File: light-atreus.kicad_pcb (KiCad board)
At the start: 2 copper layers, 40.1 x 44.5 mm, 10 parts, among them J1 USB_B, J11 USB_B, J2 CONN_01X02, J3 CONN_01X02, J4 CONN_01X02, J5 CONN_01X02, J6 CONN_01X02, J7 CONN_01X02, J8 CONN_01X02, J9 CONN_01X02

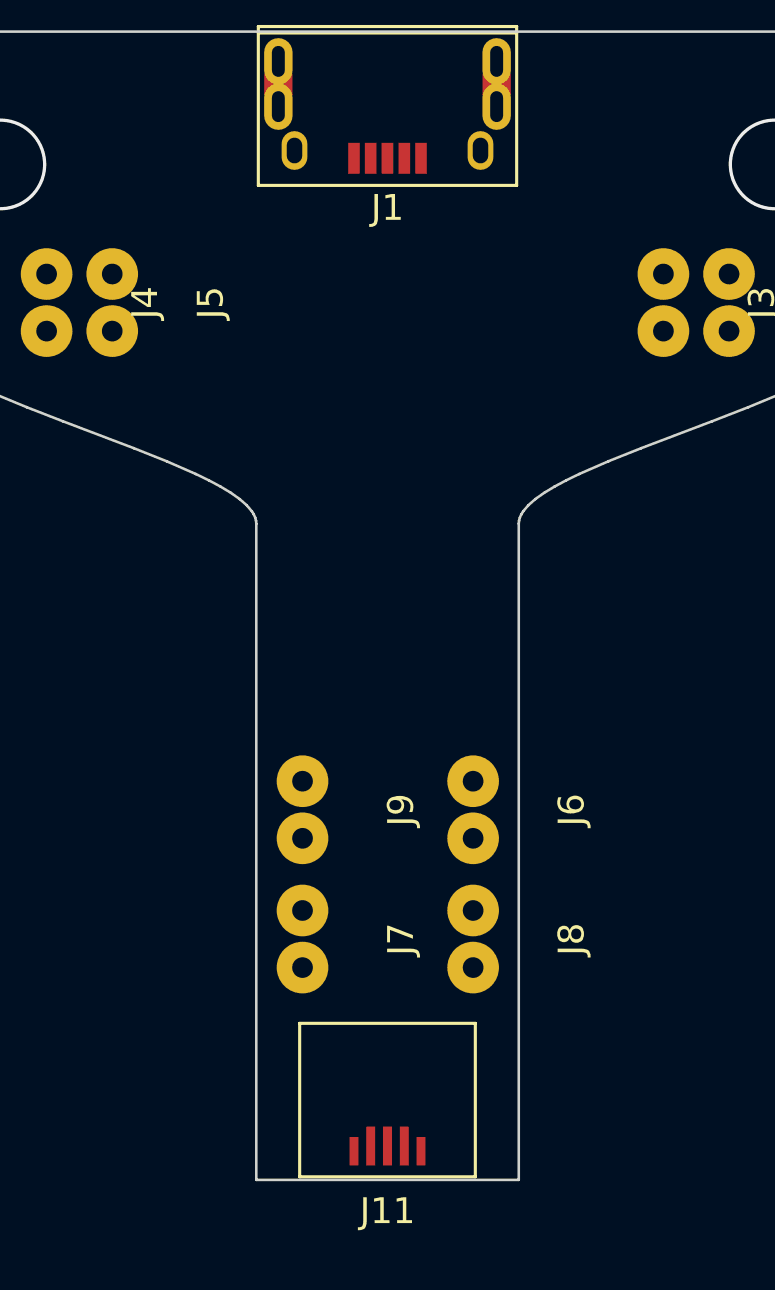
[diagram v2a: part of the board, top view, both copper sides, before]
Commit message: Wire USB header traces straight through
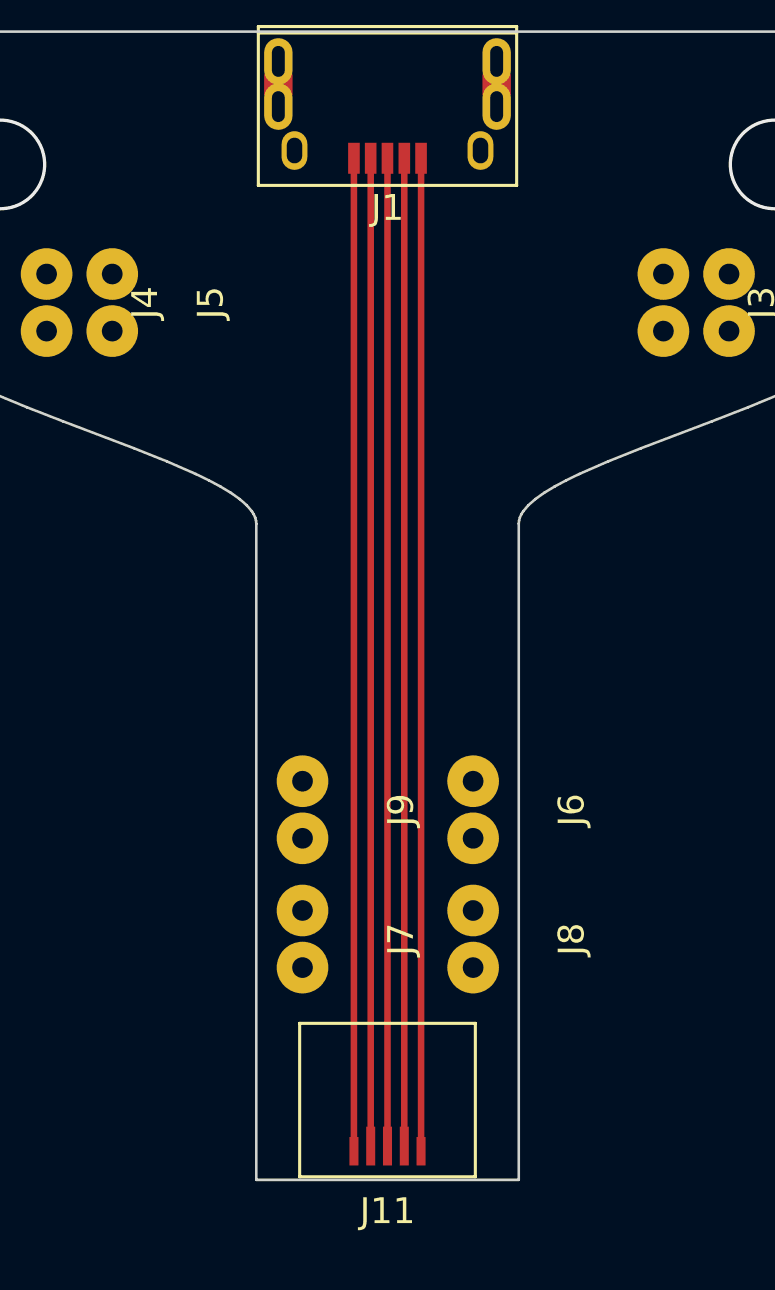
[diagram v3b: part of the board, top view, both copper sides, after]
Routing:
- net /VBUS: track 0.00 -> 38.4 mm
- net /SHIELD: track 0.00 -> 38.4 mm
- net /GND: track 0.00 -> 38.2 mm
- net /D-: track 0.00 -> 38.2 mm
- net /D+: track 0.00 -> 38.2 mm
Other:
- net class Default: clearance 0 -> 0.254; trace_width 0.2032 -> 0.254
- rule trace_clearance: 0 -> 0.254
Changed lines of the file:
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@@
     (thickness 1.6)
     (drawings 66)
-    (tracks 2)
+    (tracks 7)
     (zones 0)
     (modules 10)
@@
   )
   (setup
-    (last_trace_width 0.2032)
-    (trace_clearance 0)
+    (last_trace_width 0.254)
+    (trace_clearance 0.254)
     (zone_clearance 0.508)
     (zone_45_only no)
@@
   (net 13 "Net-(J9-Pad2)")
   (net_class Default "This is the default net class."
-    (clearance 0)
-    (trace_width 0.2032)
+    (clearance 0.254)
+    (trace_width 0.254)
     (via_dia 0.889)
     (via_drill 0.635)
@@
   (via (at 145.2753 76.0222) (size 3.556) (drill 3.302) (layers F.Cu B.Cu) (net 0) (status 40000))
   (via (at 115.3033 76.0222) (size 3.556) (drill 3.302) (layers F.Cu B.Cu) (net 0) (status 40000))
+  (segment (start 128.9893 114.2206) (end 128.9893 75.784) (width 0.254) (layer F.Cu) (net 1))
+  (segment (start 129.6393 75.784) (end 129.6393 114.0206) (width 0.254) (layer F.Cu) (net 2))
+  (segment (start 130.2893 75.784) (end 130.2893 114.0206) (width 0.254) (layer F.Cu) (net 3))
+  (segment (start 130.9393 75.784) (end 130.9393 114.0206) (width 0.254) (layer F.Cu) (net 4))
+  (segment (start 131.5893 75.784) (end 131.5893 114.2206) (width 0.254) (layer F.Cu) (net 5))
 )

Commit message: Finish routing the board
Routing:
- net /VBUS: track 38.4 -> 75.9 mm
- net /D+: track 38.2 -> 41.5 mm, vias 0 -> 1
- net /D-: track 38.2 -> 41.2 mm, vias 0 -> 1
- net /GND: track 38.2 -> 40.5 mm, vias 0 -> 2
- added copper zone on B.Cu, net /GND
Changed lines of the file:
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@@
     (thickness 1.6)
     (drawings 66)
-    (tracks 7)
+    (tracks 51)
     (zones 0)
     (modules 10)
@@
   (via (at 145.2753 76.0222) (size 3.556) (drill 3.302) (layers F.Cu B.Cu) (net 0) (status 40000))
   (via (at 115.3033 76.0222) (size 3.556) (drill 3.302) (layers F.Cu B.Cu) (net 0) (status 40000))
-  (segment (start 128.9893 114.2206) (end 128.9893 75.784) (width 0.254) (layer F.Cu) (net 1))
-  (segment (start 129.6393 75.784) (end 129.6393 114.0206) (width 0.254) (layer F.Cu) (net 2))
+  (segment (start 128.9893 76.159) (end 128.9893 75.784) (width 0.254) (layer F.Cu) (net 1))
+  (segment (start 128.460498 76.687802) (end 128.9893 76.159) (width 0.254) (layer F.Cu) (net 1))
+  (segment (start 128.9893 113.4166) (end 128.460498 112.887798) (width 0.254) (layer F.Cu) (net 1))
+  (segment (start 128.460498 112.887798) (end 128.460498 76.687802) (width 0.254) (layer F.Cu) (net 1))
+  (segment (start 128.9893 114.2206) (end 128.9893 113.4166) (width 0.254) (layer F.Cu) (net 1))
+  (segment (start 129.6393 100.076) (end 129.6393 104.139758) (width 0.254) (layer F.Cu) (net 2))
+  (segment (start 129.6393 100.076) (end 129.54 100.076) (width 0.254) (layer F.Cu) (net 2))
+  (segment (start 129.6393 75.784) (end 129.6393 100.076) (width 0.254) (layer F.Cu) (net 2))
+  (segment (start 129.54 100.076) (end 129.286 99.822) (width 0.254) (layer F.Cu) (net 2))
+  (via (at 129.286 99.822) (size 0.889) (drill 0.635) (layers F.Cu B.Cu) (net 2))
+  (segment (start 129.6393 105.664242) (end 129.6393 113.0166) (width 0.254) (layer F.Cu) (net 2))
+  (segment (start 129.273299 105.298241) (end 129.6393 105.664242) (width 0.254) (layer F.Cu) (net 2))
+  (segment (start 129.273299 104.505759) (end 129.273299 105.298241) (width 0.254) (layer F.Cu) (net 2))
+  (segment (start 129.6393 104.139758) (end 129.273299 104.505759) (width 0.254) (layer F.Cu) (net 2))
+  (segment (start 129.6393 113.0166) (end 129.6393 114.0206) (width 0.254) (layer F.Cu) (net 2))
+  (segment (start 129.6393 75.784) (end 129.6393 74.3435) (width 0.254) (layer F.Cu) (net 2))
+  (segment (start 129.6393 74.3435) (end 129.6162 74.3204) (width 0.254) (layer F.Cu) (net 2))
+  (via (at 129.6162 74.3204) (size 0.889) (drill 0.635) (layers F.Cu B.Cu) (net 2))
+  (segment (start 127 104.902) (end 130.0988 104.902) (width 0.254) (layer B.Cu) (net 3))
+  (segment (start 130.2766 104.902) (end 130.0988 104.902) (width 0.254) (layer B.Cu) (net 3))
+  (via (at 130.0988 104.902) (size 0.889) (drill 0.635) (layers F.Cu B.Cu) (net 3))
   (segment (start 130.2893 75.784) (end 130.2893 114.0206) (width 0.254) (layer F.Cu) (net 3))
-  (segment (start 130.9393 75.784) (end 130.9393 114.0206) (width 0.254) (layer F.Cu) (net 4))
-  (segment (start 131.5893 75.784) (end 131.5893 114.2206) (width 0.254) (layer F.Cu) (net 5))
+  (segment (start 133.604 104.902) (end 132.1562 104.902) (width 0.254) (layer B.Cu) (net 4))
+  (segment (start 132.1562 104.902) (end 131.1402 103.886) (width 0.254) (layer B.Cu) (net 4))
+  (via (at 131.1402 103.886) (size 0.889) (drill 0.635) (layers F.Cu B.Cu) (net 4))
+  (segment (start 130.975101 112.980799) (end 130.9393 113.0166) (width 0.254) (layer F.Cu) (net 4))
+  (segment (start 130.9393 76.638) (end 130.975101 76.673801) (width 0.254) (layer F.Cu) (net 4))
+  (segment (start 130.9393 75.784) (end 130.9393 76.638) (width 0.254) (layer F.Cu) (net 4))
+  (segment (start 130.9393 113.0166) (end 130.9393 114.0206) (width 0.254) (layer F.Cu) (net 4))
+  (segment (start 130.975101 76.673801) (end 130.975101 112.980799) (width 0.254) (layer F.Cu) (net 4))
+  (segment (start 117.094 80.264) (end 120.74299 76.61501) (width 0.254) (layer F.Cu) (net 5))
+  (segment (start 120.74299 76.61501) (end 127.054226 76.61501) (width 0.254) (layer F.Cu) (net 5))
+  (segment (start 131.5893 73.8551) (end 131.5893 75.784) (width 0.254) (layer F.Cu) (net 5))
+  (segment (start 127.054226 76.61501) (end 128.383299 75.285937) (width 0.254) (layer F.Cu) (net 5))
+  (segment (start 128.383299 75.285937) (end 128.383299 73.902301) (width 0.254) (layer F.Cu) (net 5))
+  (segment (start 128.383299 73.902301) (end 129.2352 73.0504) (width 0.254) (layer F.Cu) (net 5))
+  (segment (start 129.2352 73.0504) (end 130.7846 73.0504) (width 0.254) (layer F.Cu) (net 5))
+  (segment (start 130.7846 73.0504) (end 131.5893 73.8551) (width 0.254) (layer F.Cu) (net 5))
+  (segment (start 143.51 80.264) (end 139.884 76.638) (width 0.254) (layer F.Cu) (net 5))
+  (segment (start 139.884 76.638) (end 132.0683 76.638) (width 0.254) (layer F.Cu) (net 5))
+  (segment (start 132.0683 76.638) (end 132.0683 97.0026) (width 0.254) (layer F.Cu) (net 5))
+  (segment (start 132.0683 97.0026) (end 132.0683 112.9376) (width 0.254) (layer F.Cu) (net 5))
+  (segment (start 133.604 99.898) (end 133.604 98.484508) (width 0.254) (layer F.Cu) (net 5))
+  (segment (start 133.604 98.484508) (end 132.122092 97.0026) (width 0.254) (layer F.Cu) (net 5))
+  (segment (start 132.122092 97.0026) (end 132.0683 97.0026) (width 0.254) (layer F.Cu) (net 5))
+  (segment (start 131.5893 113.4166) (end 131.5893 114.2206) (width 0.254) (layer F.Cu) (net 5))
+  (segment (start 132.0683 112.9376) (end 131.5893 113.4166) (width 0.254) (layer F.Cu) (net 5))
+  (segment (start 131.5893 76.159) (end 132.0683 76.638) (width 0.254) (layer F.Cu) (net 5))
+  (segment (start 131.5893 75.784) (end 131.5893 76.159) (width 0.254) (layer F.Cu) (net 5))
+  (zone (net 2) (net_name /GND) (layer B.Cu) (hatch edge 0.508)
+    (connect_pads (clearance 0.508))
+    (min_thickness 0.254)
+    (fill yes (arc_segments 16) (thermal_gap 0.508) (thermal_bridge_width 0.508))
+    (polygon
+      (pts
+        (xy 115.824 84.074) (xy 125.984 87.884) (xy 125.984 114.554) (xy 134.62 114.554) (xy 134.62 87.884)
+        (xy 144.78 84.074) (xy 149.606 81.28) (xy 149.606 71.628) (xy 110.998 71.628) (xy 110.998 81.28)
+      )
+    )
+  )
 )
